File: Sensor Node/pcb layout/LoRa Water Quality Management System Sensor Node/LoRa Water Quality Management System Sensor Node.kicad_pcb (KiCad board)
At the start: 4 copper layers, 100 x 80 mm, 145 parts, among them J1 OQ0332510000G, J10 Conn_01x03, J11 CONBNC002, J2 OQ0232510000G, J3 OQ0332510000G, J5 OQ0332510000G, J6 Conn_01x02, J7 USB_B, J8 SMA-J-P-X-RA-TH1, J9 Conn_01x02, SW1 Tactile Pushbutton, U1 TMUX1309, U10 TPS63000, U11 LMV324, U12 MCP4651T-503E/ML, U13 MCP4651T-503E/ML, U2 LSF0102, U3 TMUX1309, U4 Core1262 HF, U5 MX25L3233FM2I-08Q, U6 MCP3425Axx-xCH, U7 W25Q128JVSIQ TR, U8 RP2350_60QFN, U9 TPS63000, Y1 ABM8-272-T3

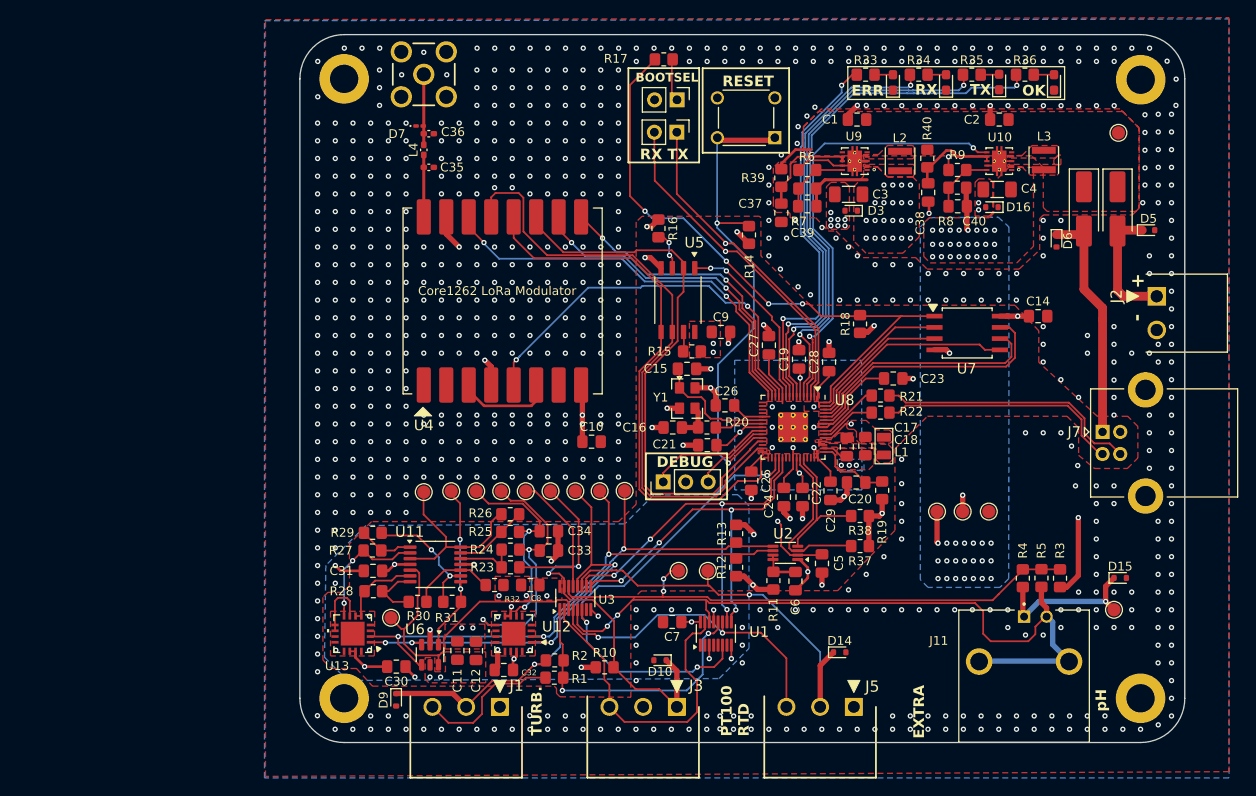
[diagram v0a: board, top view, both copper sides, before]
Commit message: Board Cleanup
Cleanup traces, fix minor layout issues. Create updated BOM
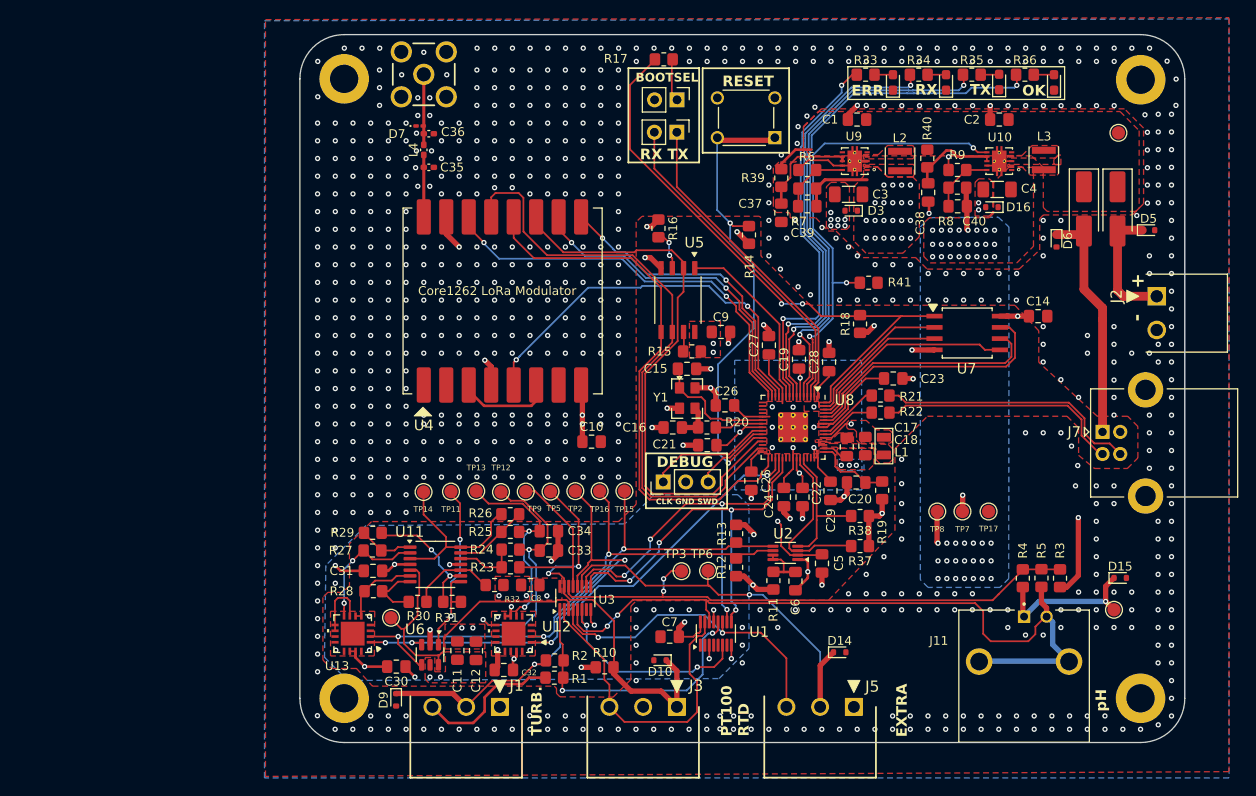
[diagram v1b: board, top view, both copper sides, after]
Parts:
- added R41: 100k, Resistor_SMD:R_0805_2012Metric_Pad1.20x1.40mm_HandSolder, F.Cu at (170.3, 85.9)
- moved C7 1.69 mm to (147.8, 125.9)
- moved TP3 0.33 mm to (149.2, 118.5)
- moved TP12 0.09 mm to (128.8, 109.5)
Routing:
- net /Software-Defined Instrumentation Amplifier/OUT: track 18.8 -> 24.8 mm
- net +5V: track 32.6 -> 35.9 mm
- net /5V_EN: track 50.7 -> 53.7 mm, vias 2 -> 3
- net /MCU/QSPI_SS: track 70.4 -> 67.5 mm, vias 4 -> 2
- net /TURB_IN: track 50.0 -> 52.5 mm
- net /SENSOR_SEL_1: track 42.8 -> 44.8 mm
- net GND: track 79.7 -> 81.2 mm, vias 779 -> 797
- net /MCU/~{RESET}: track 55.7 -> 54.2 mm
- net /SENSOR_SEL_0: track 43.9 -> 45.4 mm
- net Net-(U2-EN): track 4.42 -> 5.43 mm
- net /UART_RX_{0}: track 38.4 -> 37.7 mm, vias 1 -> 0
- net /EXTRA_IN: track 46.6 -> 47.3 mm
- net /I2C_SCL_{1}: track 15.4 -> 16.1 mm
- net /RTD_GND: track 37.3 -> 36.6 mm
- net /UART_TX_{0}: track 37.3 -> 36.7 mm, vias 1 -> 0
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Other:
- board text added: "CLK GND SWD"

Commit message: Minor modifications to PCB design, add prototyping design for signal conditioner. Finalize documentation for the first draft PCB.
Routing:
- net +3V3: track 93.0 -> 99.5 mm
- net GND: vias 797 -> 788
- net /V_{IN}: vias 0 -> 24

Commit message: Finalize PCB for order
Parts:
- removed the C11 at (123.8, 127.5)
- removed the C12 at (125.9, 127.5)
- removed the C30 at (116.9, 129.3)
- removed the C31 at (114.3, 118.5)
- removed the C32 at (129.1, 129.7)
- removed the C33 at (134.2, 116.2)
- removed the C34 at (134.2, 114.0)
- removed the C8 at (132.1, 120.1)
- removed the D1 at (198.4, 77.6)
- removed D16: T5V0S5A-7, Diode_SMD:D_SOD-523
- removed the D2 at (194.6, 77.6)
- removed the G*** at (184.2, 107.0)
- removed J11: CONBNC002, LWQMS:LINX_CONBNC002
- removed the R1 at (134.8, 130.5)
- removed the R10 at (140.5, 129.4)
- removed the R23 at (129.8, 118.1)
- removed the R24 at (129.8, 116.1)
- removed the R25 at (129.8, 114.1)
- removed the R26 at (129.8, 112.1)
- removed the R27 at (114.2, 116.2)
- removed the R28 at (114.3, 120.8)
- removed the R4 at (187.7, 119.3)
- removed the R5 at (189.8, 119.3)
- removed the TP13 at (126.0, 109.5)
- removed U1: TMUX1309, Package_SO:Texas_DYY0016A_TSOT-23-16_2x4.2mm_P0.5mm
- removed the U3 at (137.1, 121.5)
- added A1: RaspberryPi_Pico, Module:RaspberryPi_Pico_Common_Unspecified, F.Cu at (97.0, 112.3)
- added C10: 100n, Capacitor_SMD:C_0805_2012Metric_Pad1.18x1.45mm_HandSolder, F.Cu at (154.8, 123.0)
- added C15: 100n, Capacitor_SMD:C_0805_2012Metric_Pad1.18x1.45mm_HandSolder, F.Cu at (124.3, 127.0)
- added C35: 2.2n, Capacitor_SMD:C_0805_2012Metric_Pad1.18x1.45mm_HandSolder, F.Cu at (178.4, 104.2)
- added C36: 1u, Capacitor_SMD:C_0805_2012Metric_Pad1.18x1.45mm_HandSolder, F.Cu at (187.3, 104.1)
- added C37: 100u, Capacitor_SMD:C_1206_3216Metric_Pad1.33x1.80mm_HandSolder, B.Cu at (199.9, 118.2)
- added C38: 100u, Capacitor_SMD:C_1206_3216Metric_Pad1.33x1.80mm_HandSolder, B.Cu at (185.4, 117.8)
- added C39: 100n, Capacitor_SMD:C_0805_2012Metric_Pad1.18x1.45mm_HandSolder, F.Cu at (188.3, 116.9)
- added C40: 100n, Capacitor_SMD:C_0805_2012Metric_Pad1.18x1.45mm_HandSolder, F.Cu at (178.4, 109.4)
- added C41: 100n, Capacitor_SMD:C_0805_2012Metric_Pad1.18x1.45mm_HandSolder, F.Cu at (153.0, 119.5)
- added C42: 100n, Capacitor_SMD:C_0805_2012Metric_Pad1.18x1.45mm_HandSolder, F.Cu at (119.9, 122.6)
- added C43: 100n, Capacitor_SMD:C_0805_2012Metric_Pad1.18x1.45mm_HandSolder, F.Cu at (122.7, 112.0)
- added C44: 100n, Capacitor_SMD:C_0805_2012Metric_Pad1.18x1.45mm_HandSolder, F.Cu at (150.7, 123.0)
- added C45: 100n, Capacitor_SMD:C_0805_2012Metric_Pad1.18x1.45mm_HandSolder, F.Cu at (138.1, 116.1)
- added C46: 100n, Capacitor_SMD:C_0805_2012Metric_Pad1.18x1.45mm_HandSolder, F.Cu at (138.5, 127.7)
- added C47: 100n, Capacitor_SMD:C_0805_2012Metric_Pad1.18x1.45mm_HandSolder, F.Cu at (140.5, 124.1)
- added C48: 100u, Capacitor_SMD:C_1206_3216Metric_Pad1.33x1.80mm_HandSolder, B.Cu at (190.3, 112.6)
- added D4: B240AE-13, Diode_SMD:D_SMA_Handsoldering, F.Cu at (198.4, 77.6)
- added D5: B240AE-13, Diode_SMD:D_SMA_Handsoldering, F.Cu at (194.6, 77.6)
- added D8: T5V0S5A-7, Diode_SMD:D_SOD-523, F.Cu at (185.8, 84.0)
- added G***: LOGO, LOGO, F.Cu at (98.0, 71.9)
- added J3: CONBNC002, LWQMS:LINX_CONBNC002, F.Cu at (187.7, 128.7)
- added R33: 60k, Resistor_SMD:R_0805_2012Metric_Pad1.20x1.40mm_HandSolder, F.Cu at (178.4, 113.6)
- added R34: 30k, Resistor_SMD:R_0805_2012Metric_Pad1.20x1.40mm_HandSolder, F.Cu at (184.0, 120.9)
- added R35: 10k, Resistor_SMD:R_0805_2012Metric_Pad1.20x1.40mm_HandSolder, F.Cu at (131.6, 120.1)
- added R36: 10k, Resistor_SMD:R_0805_2012Metric_Pad1.20x1.40mm_HandSolder, F.Cu at (131.6, 118.1)
- added R37: 10k, Resistor_SMD:R_0805_2012Metric_Pad1.20x1.40mm_HandSolder, F.Cu at (131.6, 116.1)
- added R38: 10k, Resistor_SMD:R_0805_2012Metric_Pad1.20x1.40mm_HandSolder, F.Cu at (131.6, 114.1)
- added R39: 10k, Resistor_SMD:R_0805_2012Metric_Pad1.20x1.40mm_HandSolder, F.Cu at (116.0, 116.1)
- added R40: 10k, Resistor_SMD:R_0805_2012Metric_Pad1.20x1.40mm_HandSolder, F.Cu at (116.0, 119.1)
- added R41: 10k, Resistor_SMD:R_0805_2012Metric_Pad1.20x1.40mm_HandSolder, F.Cu at (116.0, 114.1)
- added R42: 10k, Resistor_SMD:R_0805_2012Metric_Pad1.20x1.40mm_HandSolder, F.Cu at (116.0, 123.4)
- added R43: 10k, Resistor_SMD:R_0805_2012Metric_Pad1.20x1.40mm_HandSolder, F.Cu at (131.6, 122.1)
- added R44: 10k, Resistor_SMD:R_0805_2012Metric_Pad1.20x1.40mm_HandSolder, F.Cu at (116.0, 121.4)
- added R45: 100R, Resistor_SMD:R_0805_2012Metric_Pad1.20x1.40mm_HandSolder, F.Cu at (143.6, 123.1)
- added R8: 100R, Resistor_SMD:R_0805_2012Metric_Pad1.20x1.40mm_HandSolder, F.Cu at (156.9, 125.0)
- added TP15: TestPoint_Small, TestPoint:TestPoint_Pad_D1.5mm, F.Cu at (137.0, 110.6)
- added TP18: TestPoint_Small, TestPoint:TestPoint_Pad_D1.5mm, F.Cu at (178.6, 123.4)
- added U14: LMV324, Package_SO:TSSOP-14_4.4x5mm_P0.65mm, F.Cu at (123.7, 116.1)
- added U15: MCP4651T-503E_ST, Package_SO:TSSOP-14_4.4x5mm_P0.65mm, F.Cu at (117.9, 127.6)
- added U16: MCP4651T-503E_ST, Package_SO:TSSOP-14_4.4x5mm_P0.65mm, F.Cu at (132.7, 126.9)
- added U2: TMUX1309, Package_SO:TSSOP-16_4.4x5mm_P0.65mm, F.Cu at (147.9, 127.0)
- C7: value 100n -> 4.7u
- R10: renamed from R37; value 4k -> 1k
- R13: renamed from R12; value 4k -> 1k
- R14: renamed from R13; value 4k -> 1k
- R17: renamed from R33; value 70R -> 75R
- R18: renamed from R34; value 160R -> 165R
- R19: renamed from R35; value 160R -> 165R
- R2: value 4.7k -> 0R; moved to B.Cu
- R20: renamed from R36; value 160R -> 165R
- R29: value 10k -> 4.7M
- R3: value 10k -> 4.7k; moved to B.Cu
- R30: value 10k -> 3k
- R31: value 10k -> 1k
- R32: value 10k -> 30k
- R6: renamed from R8; value 900k -> 910k
- R9: renamed from R38; value 4k -> 1k
- TP12, TP14: value TestPoint_Small -> TestPoint
- TP16, TP17: value TestPoint -> TestPoint_Small
- U11: value LMV324 -> TL082; footprint Package_SO:TSSOP-14_4.4x5mm_P0.65mm -> LWQMS:SOIC_208MIL_WIN-M
- U12: value MCP4651T-503E/ML -> LM2660MX; footprint LWQMS:QFN16_4x4MC_MCH-M -> LWQMS:SOIC_208MIL_WIN-M; moved to B.Cu
- U13: value MCP4651T-503E/ML -> MCP4651T-503E_ST; footprint LWQMS:QFN16_4x4MC_MCH-M -> Package_SO:TSSOP-14_4.4x5mm_P0.65mm
- U3: renamed from U2; footprint Package_SO:VSSOP-8_2.3x2mm_P0.5mm -> Package_SO:TSSOP-8_3x3mm_P0.65mm
- moved TP17 68.4 mm to (115.5, 109.9)
- moved R30 68.1 mm to (185.1, 104.2), turned to 90 degrees
- moved R29 67.1 mm to (180.6, 104.2), turned to -90 degrees
- moved R3 66.3 mm to (126.3, 129.0)
- moved U12 62.8 mm to (192.5, 117.4)
- moved R31 62.2 mm to (182.9, 104.2), turned to -90 degrees
- moved U11 62.2 mm to (183.4, 114.2), turned to -90 degrees
- moved R32 60.9 mm to (188.3, 111.5), turned to -90 degrees
- moved TP2 56.5 mm to (192.6, 120.2)
- moved TP9 48.2 mm to (178.6, 119.9)
- moved TP5 42.5 mm to (175.6, 119.9)
- moved TP3 39.8 mm to (110.1, 126.1)
- moved U13 35.1 mm to (146.5, 118.9), turned to 0 degrees
- moved REF** 30.0 mm to (81.0, 132.9)
- moved REF** 30.0 mm to (81.0, 62.9)
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- renumbered C9 to C11, C10 to C12, C35 to C14, C36 to C16, C14 to C17, C15 to C18, C16 to C19, C17 to C20, C18 to C21, C19 to C22, C20 to C23, C21 to C24, C22 to C25, C23 to C26, C24 to C27, C25 to C28, C26 to C29, C39 to C3, C27 to C30, C28 to C31, C29 to C32, C37 to C33, C38 to C34, C3 to C4, C40 to C5, C4 to C6, C5 to C8, C6 to C9, D5 to D1, D14 to D10, D8 to D11, D11 to D12, D7 to D13, D12 to D14, D13 to D15, D6 to D2, D15 to D3, D9 to D6, D3 to D7, D10 to D9, J3 to J4, L4 to L1, L1 to L2, L2 to L3, L3 to L4, R41 to R1, R14 to R11, R11 to R12, R17 to R21, R18 to R22, R19 to R23, R20 to R24, R21 to R25, R22 to R26, R39 to R27, R40 to R28, R6 to R4, R7 to R5, R9 to R7, TP15 to TP13
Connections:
- J4 pad 3: /RTD_GND -> GND
- J5 pad 3: /EXTRA_GND -> GND
- R2 pad 1: /TURB_IN -> Net-(J1-Pin_3)
- R2 pad 2: /TURB_GND -> GND
- R29 pad 1: Net-(R27-Pad1) -> /PH_RAW
- R29 pad 2: Net-(U11C--) -> Net-(U11A-+)
- R3 pad 1: +3V3 -> /TURB_IN
- R3 pad 2: /PH_IN -> GND
- R30 pad 1: Net-(R28-Pad2) -> Net-(U11A--)
- R30 pad 2: Net-(U11C-+) -> Net-(C36-Pad2)
- R31 pad 1: Net-(U11C--) -> GND
- R31 pad 2: /Software-Defined Instrumentation Amplifier/OUT -> Net-(U11A--)
- R32 pad 1: Net-(U11C-+) -> Net-(C36-Pad2)
- R32 pad 2: GND -> Net-(U11B--)
- TP1 pad 1: /PH_RAW -> GND
- TP10 pad 1: /Software-Defined Instrumentation Amplifier/IN- -> /Software-Defined Instrumentation Amplifier/IN+
- TP11 pad 1: /Software-Defined Instrumentation Amplifier/OUT -> /Software-Defined Instrumentation Amplifier/IN-
- TP12 pad 1: /Software-Defined Instrumentation Amplifier/V_{offset+} -> /I2C_SDA_{1}_5V
- TP14 pad 1: /Software-Defined Instrumentation Amplifier/V_SENSOR_WITH_DC_OFFSET -> /Software-Defined Instrumentation Amplifier/OUT
- TP16 pad 1: /I2C_SDA_{1}_5V -> /Software-Defined Instrumentation Amplifier/V_{offset-}
- TP17 pad 1: GND -> /Software-Defined Instrumentation Amplifier/V_SENSOR_WITH_DC_OFFSET
- TP2 pad 1: /TURB_IN -> /PH_RAW
- TP3 pad 1: /PH_IN -> /TURB_IN
- TP5 pad 1: /RTD_SEN -> +3V3
- TP6 pad 1: /EXTRA_IN -> /PH_IN
- TP7 pad 1: +3V3 -> /RTD_SEN
- TP8 pad 1: +5V -> /EXTRA_IN
- TP9 pad 1: /Software-Defined Instrumentation Amplifier/IN+ -> +5V
- U11 pad 1: Net-(R27-Pad1) -> Net-(C36-Pad2)
- U11 pad 2: /Software-Defined Instrumentation Amplifier/RGain+ -> Net-(U11A--)
- U11 pad 3: /Software-Defined Instrumentation Amplifier/V_SENSOR_WITH_DC_OFFSET -> Net-(U11A-+)
- U11 pad 4: +5V -> /PH Sensor Pre-Amplifier ALT/-5V
- U11 pad 5: /Software-Defined Instrumentation Amplifier/IN- -> GND
- U11 pad 6: /Software-Defined Instrumentation Amplifier/RGain- -> Net-(U11B--)
- U11 pad 7: Net-(R28-Pad2) -> /PH_IN
- U11 pad 8: /Software-Defined Instrumentation Amplifier/OUT -> +5V
- U12 pad 1: /I2C_SCL_{1}_5V -> unconnected-(U12-FC-Pad1)
- U12 pad 2: /I2C_SDA_{1}_5V -> Net-(U12-CAP+)
- U12 pad 4: GND -> Net-(U12-CAP-)
- U12 pad 5: GND -> /PH Sensor Pre-Amplifier ALT/-5V
- U12 pad 6: /Software-Defined Instrumentation Amplifier/V_{offset-} -> GND
- U12 pad 7: +5V -> unconnected-(U12-OSC-Pad7)
- U13 pad 1: /I2C_SCL_{1}_5V -> GND
- U13 pad 10: Net-(U13-P0B) -> GND
- U13 pad 12: unconnected-(U13-NC-Pad12) -> GND
- U13 pad 2: /I2C_SDA_{1}_5V -> /I2C_SCL_{1}_5V
- U13 pad 3: GND -> /I2C_SDA_{1}_5V
- U13 pad 5: /Software-Defined Instrumentation Amplifier/RGain- -> GND
- U13 pad 6: /Software-Defined Instrumentation Amplifier/RGain- -> /Software-Defined Instrumentation Amplifier/V_{offset-}
- U13 pad 7: Net-(U13-P0B) -> +5V
- U13 pad 8: /Software-Defined Instrumentation Amplifier/RGain+ -> +5V
- U13 pad 9: Net-(U13-P0B) -> /Software-Defined Instrumentation Amplifier/V_{offset+}
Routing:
- net GND: track 81.2 -> 258.5 mm, vias 788 -> 1090
- net /I2C_SCL_{1}: track 16.1 -> 107.6 mm, vias 0 -> 2
- net /5V_EN: track 53.7 -> 143.4 mm, vias 3 -> 6
- net /LoRa_~{RESET}: track 37.5 -> 126.8 mm
- net /I2C_SDA_{1}: track 19.3 -> 105.6 mm, vias 0 -> 2
- net /UART_TX_{0}: track 36.7 -> 122.9 mm
- net /STATUS_LED: track 60.3 -> 145.7 mm, vias 2 -> 5
- net /PH_GND: track 84.3 -> 0.00 mm, vias 2 -> 0
- net /TX_LED: track 55.0 -> 137.2 mm, vias 2 -> 5
- net /UART_RX_{0}: track 37.7 -> 119.3 mm
- net /RX_LED: track 49.8 -> 130.0 mm, vias 2 -> 5
- net /ERR_LED: track 44.5 -> 120.6 mm, vias 2 -> 5
- net /MCU/~{RESET}: track 54.2 -> 124.0 mm, vias 2 -> 4
- net /~{FLASH_CS}: track 20.7 -> 89.9 mm, vias 0 -> 3
- net /LoRa_BUSY: track 34.9 -> 100.1 mm, vias 2 -> 4
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- added copper zone on B.Cu, net /PH Sensor Pre-Amplifier ALT/-5V
- added copper zone on F.Cu, net /PH Sensor Pre-Amplifier ALT/-5V
- added copper zone on In2.Cu, net /PH Sensor Pre-Amplifier ALT/-5V
- added copper zone on B.Cu, net Net-(U12-CAP+)
- added copper zone on B.Cu, net Net-(U12-CAP-)
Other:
- board size 100 x 80 mm -> 130 x 80 mm
- board text added: "Powered by magic smoke - do not release."
- board text added: "Rev 1.3/A"
- board text added: "WARNING: DO NOT LICK"
- board text added: "Yet another groundbreaking project by Matthew Sharp, Cole Hadley, and Patricio Benitez Palermo"
- board text removed: "Rev 1.1/A"
- board text removed: "Yet another groundbreaking project by Matthew Sharp, Cole Hadley, and Patricio Palermo"
